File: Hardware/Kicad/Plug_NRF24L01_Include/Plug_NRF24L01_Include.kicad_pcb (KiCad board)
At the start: 2 copper layers, 40 x 40 mm, 54 parts, among them J1 Conn_01x07_Socket, J2 Conn_02x07_Odd_Even, Q1 2N7002, Q2 2N7002, Q3 2N7002, Q4 2N7002, Q5 2N7002, SW2 SW_SPST, U1 STM32L412KBTx, U2 MIC5219-3.3YMM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

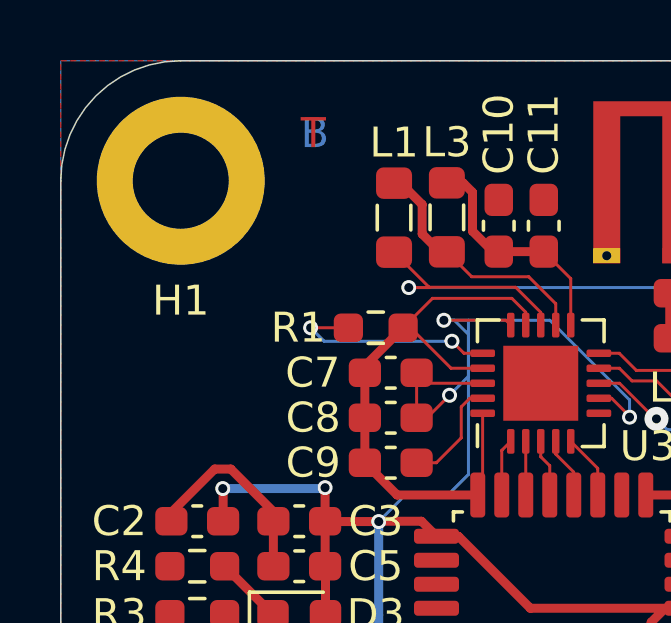
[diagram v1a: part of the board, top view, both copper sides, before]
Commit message: Updated Plug_NRF24L01 (Text, ruler, images)
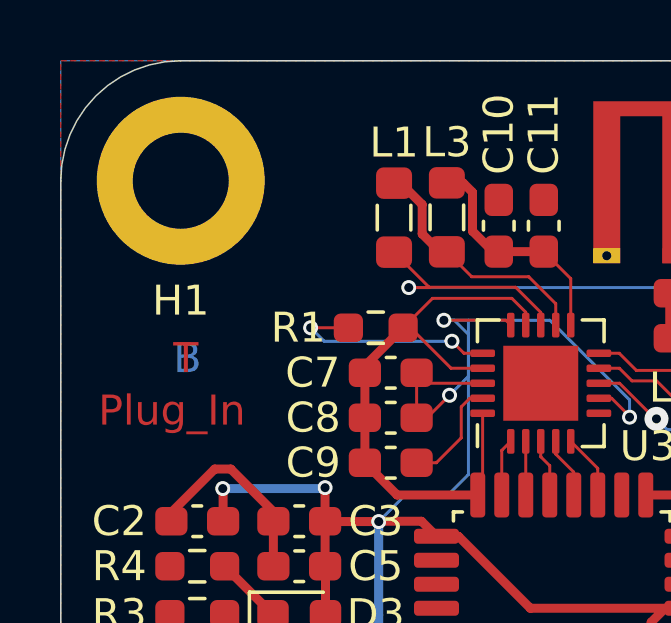
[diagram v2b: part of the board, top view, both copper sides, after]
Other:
- board text added: "Plug_In"
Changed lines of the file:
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@@
   (gr_arc (start 136 100) (mid 134.828427 102.828427) (end 132 104)
     (stroke (width 0.05) (type default)) (layer "Edge.Cuts"))
-  (gr_text "T" (at 104 67) (layer "F.Cu")
+  (gr_text "T" (at 99.75 74.5) (layer "F.Cu")
     (effects (font (size 1 1) (thickness 0.15)) (justify left bottom))
   )
-  (gr_text "B" (at 104 67) (layer "B.Cu")
+  (gr_text "Plug_In" (at 97.25 76.25) (layer "F.Cu")
+    (effects (font (size 1 1) (thickness 0.15)) (justify left bottom))
+  )
+  (gr_text "B" (at 99.75 74.5) (layer "B.Cu")
     (effects (font (size 1 1) (thickness 0.15)) (justify left bottom))
   )
   (dimension (type aligned) (layer "User.1")
-    (pts (xy 96 104) (xy 136 104))
-    (height -43)
-    (gr_text "40.0000 mm" (at 116 59.85) (layer "User.1")
+    (pts (xy 136 104) (xy 136 64))
+    (height 4)
+    (gr_text "40.0000 mm" (at 138.85 84 90) (layer "User.1")
       (effects (font (size 1 1) (thickness 0.15)))
     )
@@
   )
   (dimension (type aligned) (layer "User.1")
-    (pts (xy 96 104) (xy 96 64))
-    (height 44)
-    (gr_text "40.0000 mm" (at 138.85 84 90) (layer "User.1")
+    (pts (xy 136 64) (xy 96 64))
+    (height 4)
+    (gr_text "40.0000 mm" (at 116 58.85) (layer "User.1")
       (effects (font (size 1 1) (thickness 0.15)))
     )

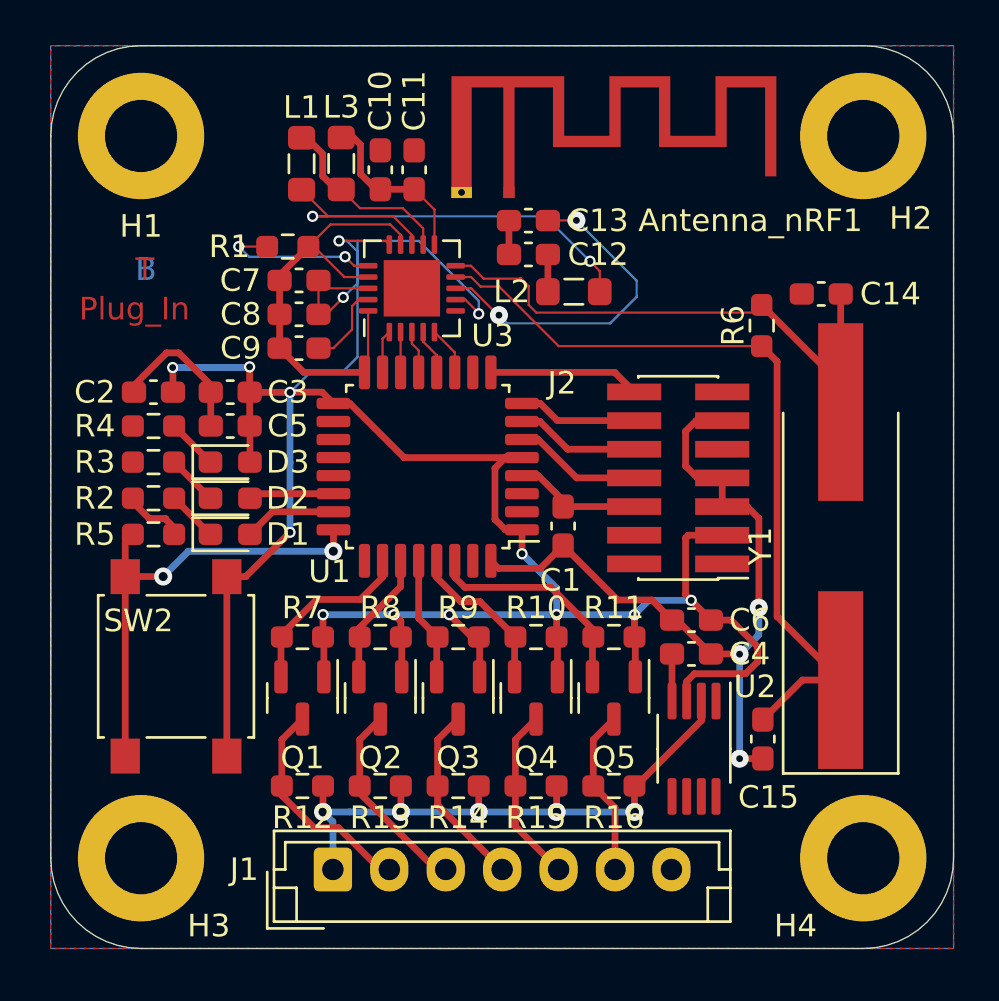
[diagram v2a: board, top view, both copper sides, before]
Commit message: Updated Plug_NRF24L01_Include (V2.1) - Schematic & PCB & Image
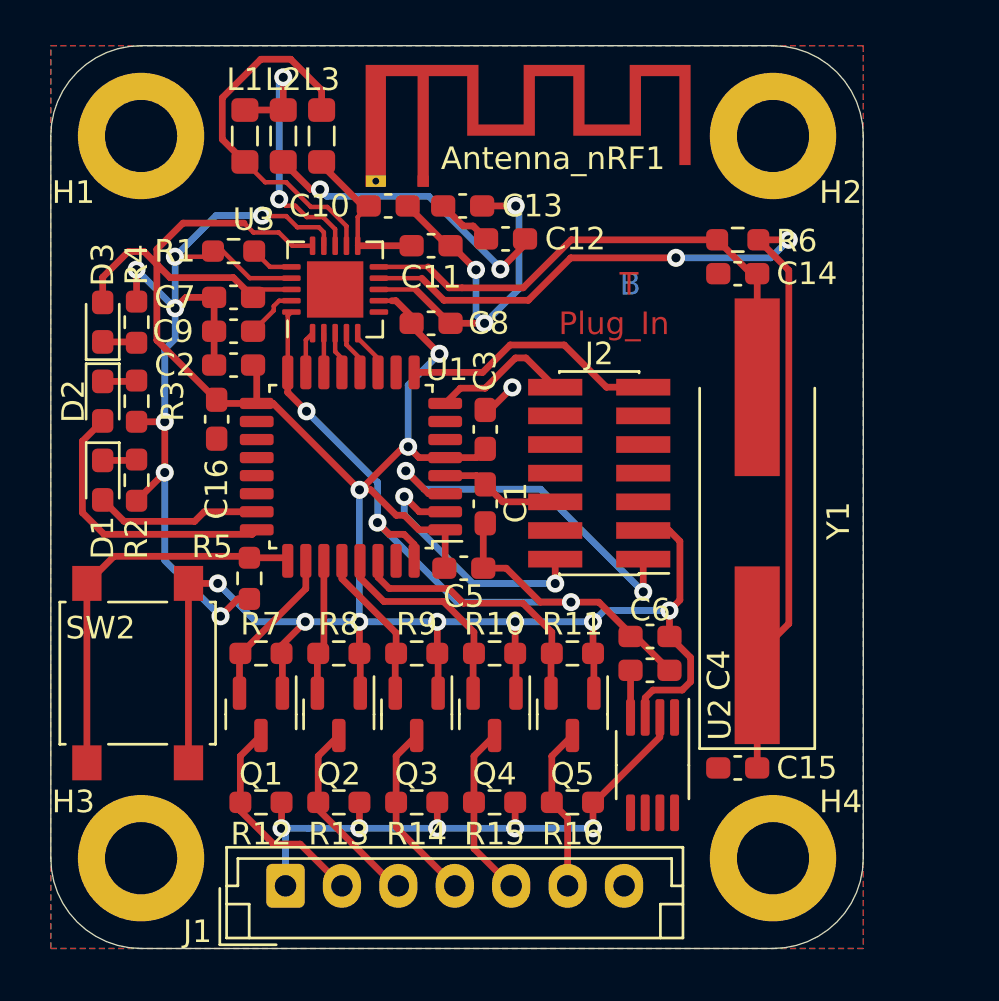
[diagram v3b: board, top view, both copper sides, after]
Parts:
- added C16: 10u, Capacitor_SMD:C_0603_1608Metric_Pad1.08x0.95mm_HandSolder, F.Cu at (103.3, 80.5)
- moved L2 14.6 mm to (106.3, 68.0), turned to -90 degrees
- moved C5 12.1 mm to (114.3, 87.2), turned to 0 degrees
- moved C3 11.4 mm to (115.2, 81.0), turned to 90 degrees
- moved D3 8.39 mm to (98.3, 76.2), turned to 90 degrees
- moved D2 7.10 mm to (98.3, 79.8), turned to -90 degrees
- moved D1 6.14 mm to (98.3, 83.2), turned to -90 degrees
- moved C8 5.86 mm to (112.8, 76.3), turned to 0 degrees
- moved R5 4.68 mm to (104.8, 87.6), turned to -90 degrees
- moved R4 4.66 mm to (99.8, 76.2), turned to 90 degrees
- moved H2 4.00 mm to (128.0, 68.0)
- moved H4 4.00 mm to (128.0, 100.0)
- moved R6 3.95 mm to (126.4, 72.6), turned to 0 degrees
- moved Y1 3.86 mm to (127.3, 85.1)
- moved Antenna_nRF1 3.83 mm to (112.5, 70.0)
- moved C14 3.81 mm to (126.4, 74.1)
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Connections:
- J2 pad 1: unconnected-(J2-Pin_1-Pad1) -> USART2_RX
- J2 pad 10: SWDCK -> unconnected-(J2-Pin_10-Pad10)
- J2 pad 12: USART2_RX -> unconnected-(J2-Pin_12-Pad12)
- J2 pad 13: unconnected-(J2-Pin_13-Pad13) -> SWDIO
- J2 pad 14: USART2_TX -> SWDCK
- J2 pad 2: unconnected-(J2-Pin_2-Pad2) -> USART2_TX
- J2 pad 8: SWDIO -> unconnected-(J2-Pin_8-Pad8)
- U1 pad 2: unconnected-(U1-PC14-Pad2) -> USART2_TX
- U1 pad 22: Status_LED -> unconnected-(U1-PA12-Pad22)
- U1 pad 24: Appairing_Btn -> Status_LED
- U1 pad 25: unconnected-(U1-PA15-Pad25) -> Appairing_Btn
- U1 pad 3: unconnected-(U1-PC15-Pad3) -> USART2_RX
- U1 pad 6: SWDIO -> unconnected-(U1-PA0-Pad6)
- U1 pad 7: SWDCK -> unconnected-(U1-PA1-Pad7)
- U1 pad 8: USART2_RX -> SWDCK
- U1 pad 9: USART2_TX -> SWDIO
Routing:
- net GND: track 78.7 -> 103.8 mm, vias 5 -> 14
- net Net-(C12-Pad2): track 1.65 -> 13.4 mm, vias 0 -> 2
- net USART2_RX: track 5.29 -> 16.4 mm, vias 0 -> 2
- net XC2: track 35.3 -> 45.6 mm, vias 0 -> 2
- net ANT2: track 21.5 -> 12.4 mm
- net Status_LED: track 3.78 -> 12.6 mm
- net ANT1: track 8.34 -> 16.4 mm
- net SWDIO: track 5.68 -> 11.4 mm
- net Net-(U3-IREF): track 7.34 -> 1.94 mm, vias 2 -> 0
- net USART2_TX: track 6.71 -> 11.9 mm, vias 0 -> 2
- net Player1_LED: track 4.11 -> 7.39 mm
- net Appairing_Btn: track 20.6 -> 17.4 mm, vias 2 -> 0
- net XC1: track 26.5 -> 23.7 mm
- net Serial_Data2_STM32: track 7.10 -> 9.51 mm
- net IOBit_STM32: track 9.93 -> 12.2 mm
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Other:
- board size 40 x 40 mm -> 36 x 40 mm
